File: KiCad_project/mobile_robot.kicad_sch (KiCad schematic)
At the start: 57 parts, among them J1 IR, J13 Encoder A, J14 Encoder B, J15 Conn_02x05_Odd_Even, J16 Conn_02x05_Odd_Even, J17 Conn_01x03_Pin, J18 Conn_01x03_Pin, J19 Conn_02x08_Odd_Even, J2 PROGRAMING, J20 i2c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

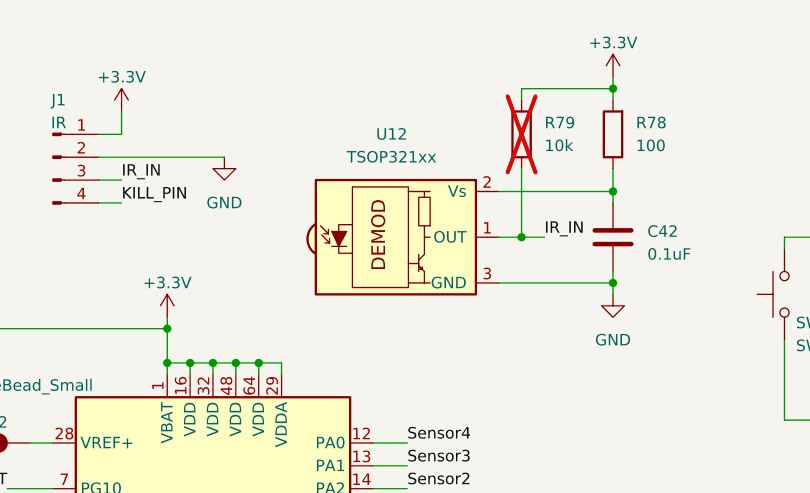
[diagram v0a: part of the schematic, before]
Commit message: update routing, changed IR sensor with pinout, rotate right sensor connector (bottom side)
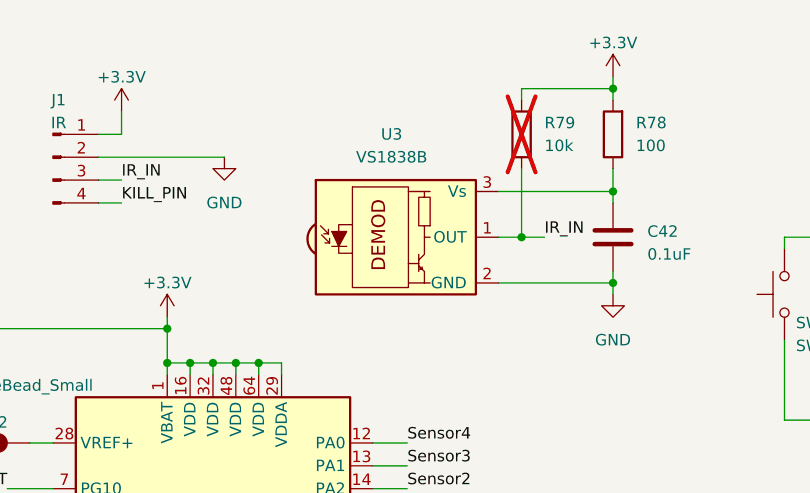
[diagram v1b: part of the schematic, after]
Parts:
- removed U12: TSOP321xx, OptoDevice:Vishay_MOLD-3Pin, symbol symbol_library:TSOP321xx
- added U3: VS1838B, footprint_library:Vishay_MOLD-3Pin, symbol symbol_library:VS1838B
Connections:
- net GND: now also U3.2 (GND)
- net IR_IN: now also U3.1 (OUT)
- net at C42.1, R78.1: now also U3.3 (Vs)
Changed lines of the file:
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@@
-	)
-	(symbol
-		(lib_id "symbol_library:TSOP321xx")
-		(at 114.3 38.1 0)
-		(unit 1)
-		(exclude_from_sim no)
-		(in_bom yes)
-		(on_board yes)
-		(dnp no)
-		(fields_autoplaced yes)
-		(property "Reference" "U12"
-			(at 112.565 26.67 0)
-			(effects
-				(font
-					(size 1.27 1.27)
-				)
-			)
-		)
-		(property "Value" "TSOP321xx"
-			(at 112.565 29.21 0)
-			(effects
-				(font
-					(size 1.27 1.27)
-				)
-			)
-		)
-		(property "Footprint" "OptoDevice:Vishay_MOLD-3Pin"
-			(at 113.03 47.625 0)
-			(effects
-				(font
-					(size 1.27 1.27)
-				)
-				(hide yes)
-			)
-		)
-		(property "Datasheet" "http://www.vishay.com/docs/82490/tsop321.pdf"
-			(at 130.81 30.48 0)
-			(effects
-				(font
-					(size 1.27 1.27)
-				)
-				(hide yes)
-			)
-		)
-		(property "Description" "IR Receiver Modules for Remote Control Systems"
-			(at 114.3 38.1 0)
-			(effects
-				(font
-					(size 1.27 1.27)
-				)
-				(hide yes)
-			)
-		)
-		(pin "1"
-		)
-		(pin "3"
-		)
-		(pin "2"
-		)
-		(instances
-			(project ""
-				(path "/e8f9f0a0-cca9-426a-b8ab-73515fe7421d"
-					(reference "U12")
-					(unit 1)
-				)
-			)
-		)
 	)
 	(symbol
@@
 					(unit 1)
 				)
+			)
+		)
+	)
+	(symbol
+		(lib_id "symbol_library:VS1838B")
+		(at 114.3 38.1 0)
+		(unit 1)
+		(exclude_from_sim no)
+		(in_bom yes)
+		(on_board yes)
+		(dnp no)
+		(fields_autoplaced yes)
+		(property "Reference" "U3"
+			(at 112.565 26.67 0)
+			(effects
+				(font
+					(size 1.27 1.27)
+				)
+			)
+		)
+		(property "Value" "VS1838B"
+			(at 112.565 29.21 0)
+			(effects
+				(font
+					(size 1.27 1.27)
+				)
+			)
+		)
+		(property "Footprint" "footprint_library:Vishay_MOLD-3Pin"
+			(at 113.03 47.625 0)
+			(effects
+				(font
+					(size 1.27 1.27)
+				)
+				(hide yes)
+			)
+		)
+		(property "Datasheet" ""
+			(at 115.57 30.226 0)
+			(effects
+				(font
+					(size 1.27 1.27)
+				)
+				(hide yes)
+			)
+		)
+		(property "Description" "IR Receiver Modules for Remote Control Systems"
+			(at 114.3 38.1 0)
+			(effects
+				(font
+					(size 1.27 1.27)
+				)
+				(hide yes)
+			)
+		)
+		(pin "1"
+		)
+		(pin "2"
+		)
+		(pin "3"
+		)
+		(instances
+			(project ""
+				(path "/e8f9f0a0-cca9-426a-b8ab-73515fe7421d"
+					(reference "U3")
+					(unit 1)
+				)

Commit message: update GND routing
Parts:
- D3: footprint Diode_SMD:D_MiniMELF_Handsoldering -> Diode_SMD:D_MiniMELF
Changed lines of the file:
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@@
 			)
 		)
-		(property "Footprint" "Diode_SMD:D_MiniMELF_Handsoldering"
+		(property "Footprint" "Diode_SMD:D_MiniMELF"
 			(at 53.34 39.37 0)
 			(effects
